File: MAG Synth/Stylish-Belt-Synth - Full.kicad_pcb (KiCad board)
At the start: 2 copper layers, 177.8 x 101.7 mm, 75 parts, among them J0 USB_B, J1 Headphone, J26 WRITE PATCH, J27 PARAM SELECT, J28 PATCH SELECT, J29 MODE, J30 STYLUS, U1 stm32f103c8t6-module-china, U2 XPT8871

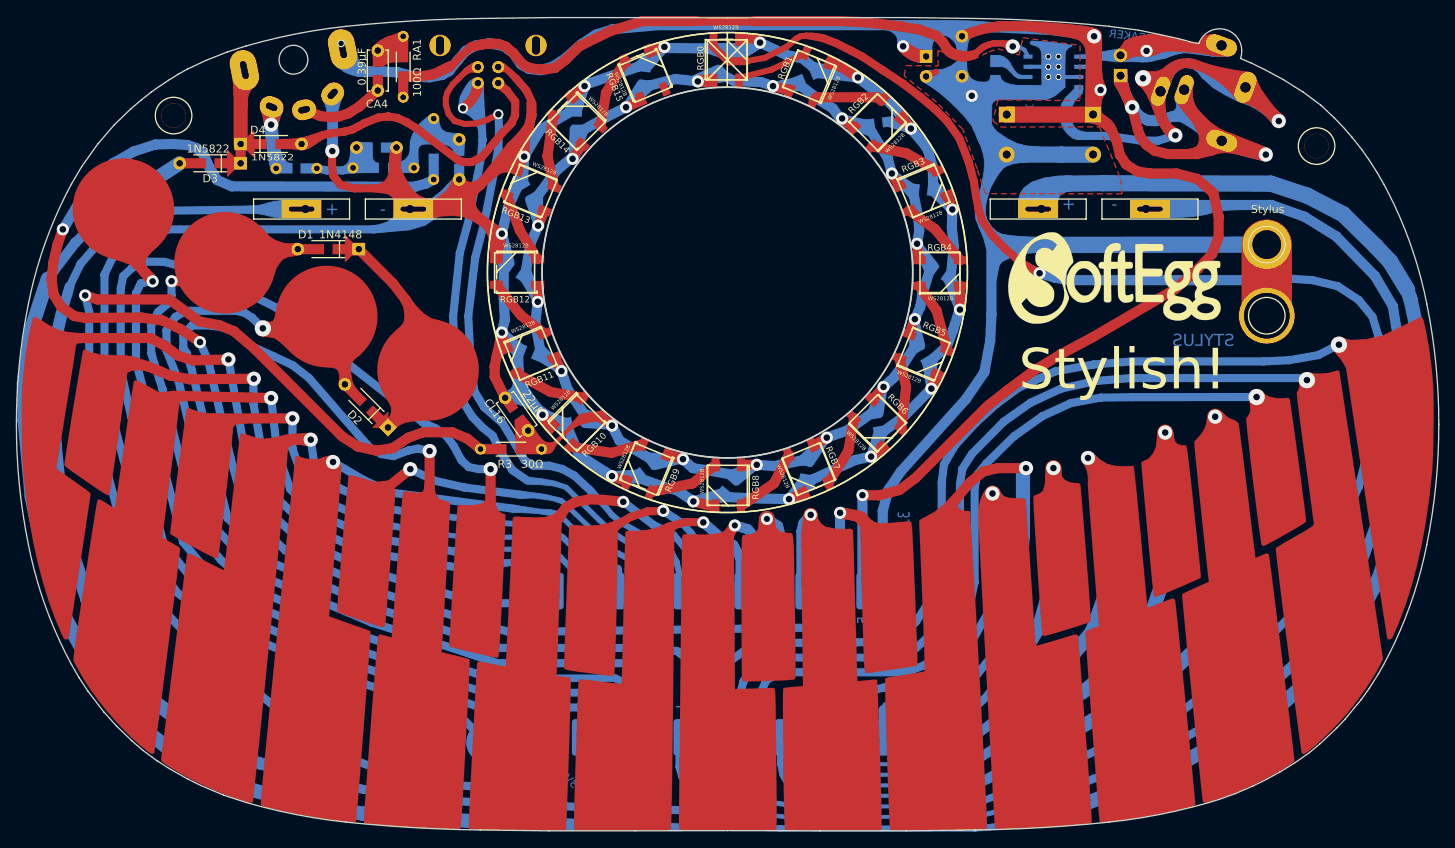
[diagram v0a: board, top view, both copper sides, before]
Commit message: Fixes for removing LED noise from the audio. Thanks Brandon for the hard work in figuring this out!
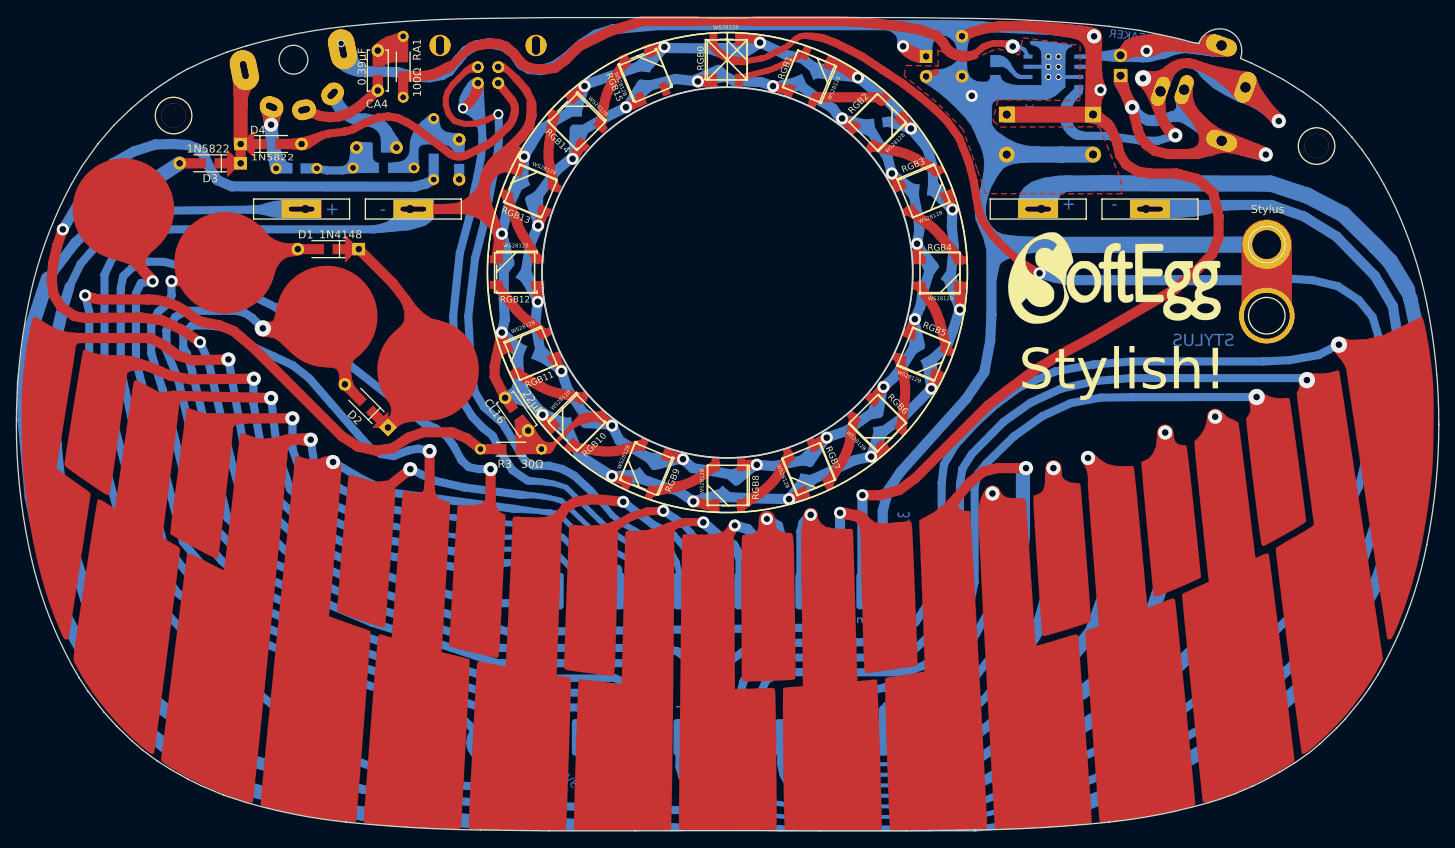
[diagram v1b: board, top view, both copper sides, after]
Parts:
- CA1: value 220μF -> 220µF
- LS1: value SPEAKER -> Speaker 4Ω 3W
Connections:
- net /DOUT renamed /WS2812B-16-LED-RING/DOUT
- BT12H1 pad 2: GND -> AGND
- BTN1 pad 1: GND -> AGND
- C1 pad 2: GND -> Net-(C1-Pad2)
- C2 pad 2: GND -> AGND
- C3 pad 2: GND -> AGND
- C4 pad 2: GND -> Net-(C4-Pad2)
- CA1 pad 2: GND -> AGND
- CA2 pad 2: GND -> AGND
- CA3 pad 2: GND -> AGND
- CL0 pad 1: /VIN -> /WS2812B-16-LED-RING/VIN
- CL0 pad 2: GND -> AGND
- CL1 pad 1: /VIN -> /WS2812B-16-LED-RING/VIN
- CL1 pad 2: GND -> AGND
- CL10 pad 1: /VIN -> /WS2812B-16-LED-RING/VIN
- CL10 pad 2: GND -> AGND
- CL11 pad 1: /VIN -> /WS2812B-16-LED-RING/VIN
- CL11 pad 2: GND -> AGND
- CL12 pad 1: /VIN -> /WS2812B-16-LED-RING/VIN
- CL12 pad 2: GND -> AGND
- CL13 pad 1: /VIN -> /WS2812B-16-LED-RING/VIN
- CL13 pad 2: GND -> AGND
- CL14 pad 1: /VIN -> /WS2812B-16-LED-RING/VIN
- CL14 pad 2: GND -> AGND
- CL15 pad 1: /VIN -> /WS2812B-16-LED-RING/VIN
- CL15 pad 2: GND -> AGND
- CL16 pad 1: /VIN -> unconnected-(CL16-Pad1)
- CL16 pad 2: GND -> AGND
- CL2 pad 1: /VIN -> /WS2812B-16-LED-RING/VIN
- CL2 pad 2: GND -> AGND
- CL3 pad 1: /VIN -> /WS2812B-16-LED-RING/VIN
- CL3 pad 2: GND -> AGND
- CL4 pad 1: /VIN -> /WS2812B-16-LED-RING/VIN
- CL4 pad 2: GND -> AGND
- CL5 pad 1: /VIN -> /WS2812B-16-LED-RING/VIN
- CL5 pad 2: GND -> AGND
- CL6 pad 1: /VIN -> /WS2812B-16-LED-RING/VIN
- CL6 pad 2: GND -> AGND
- CL7 pad 1: /VIN -> /WS2812B-16-LED-RING/VIN
- CL7 pad 2: GND -> AGND
- CL8 pad 1: /VIN -> /WS2812B-16-LED-RING/VIN
- CL8 pad 2: GND -> AGND
- CL9 pad 1: /VIN -> /WS2812B-16-LED-RING/VIN
- CL9 pad 2: GND -> AGND
- J0 pad 4: GND -> AGND
- J0 pad 5: Net-(J0-Pad5) -> unconnected-(J0-Pad5)
- J30 pad 1: GND -> AGND
- R3 pad 1: /VIN -> /WS2812B-16-LED-RING/VIN
- RGB0 pad 1: /VIN -> /WS2812B-16-LED-RING/VIN
- RGB0 pad 3: GND -> AGND
- RGB1 pad 1: /VIN -> /WS2812B-16-LED-RING/VIN
- RGB1 pad 3: GND -> AGND
- RGB10 pad 1: /VIN -> /WS2812B-16-LED-RING/VIN
- RGB10 pad 3: GND -> AGND
- RGB11 pad 1: /VIN -> /WS2812B-16-LED-RING/VIN
- RGB11 pad 3: GND -> AGND
- RGB12 pad 1: /VIN -> /WS2812B-16-LED-RING/VIN
- RGB12 pad 3: GND -> AGND
- RGB13 pad 1: /VIN -> /WS2812B-16-LED-RING/VIN
- RGB13 pad 3: GND -> AGND
- RGB14 pad 1: /VIN -> /WS2812B-16-LED-RING/VIN
- RGB14 pad 3: GND -> AGND
- RGB15 pad 1: /VIN -> /WS2812B-16-LED-RING/VIN
- RGB15 pad 3: GND -> AGND
- RGB2 pad 1: /VIN -> /WS2812B-16-LED-RING/VIN
- RGB2 pad 3: GND -> AGND
- RGB3 pad 1: /VIN -> /WS2812B-16-LED-RING/VIN
- RGB3 pad 3: GND -> AGND
- RGB4 pad 1: /VIN -> /WS2812B-16-LED-RING/VIN
- RGB4 pad 3: GND -> AGND
- RGB5 pad 1: /VIN -> /WS2812B-16-LED-RING/VIN
- RGB5 pad 3: GND -> AGND
- RGB6 pad 1: /VIN -> /WS2812B-16-LED-RING/VIN
- RGB6 pad 3: GND -> AGND
- RGB7 pad 1: /VIN -> /WS2812B-16-LED-RING/VIN
- RGB7 pad 3: GND -> AGND
- RGB8 pad 1: /VIN -> /WS2812B-16-LED-RING/VIN
- RGB8 pad 3: GND -> AGND
- RGB9 pad 1: /VIN -> /WS2812B-16-LED-RING/VIN
- RGB9 pad 3: GND -> AGND
- RV1 pad 1: GND -> Net-(C4-Pad2)
- U1 pad 19: GND -> AGND
- U1 pad 20: Net-(U1-Pad20) -> unconnected-(U1-Pad20)
- U1 pad 21: Net-(U1-Pad21) -> unconnected-(U1-Pad21)
- U1 pad 37: Net-(U1-Pad37) -> unconnected-(U1-Pad37)
- U1 pad 39: GND -> AGND
- U1 pad 40: GND -> AGND
- U2 pad 1: GND -> AGND
- U2 pad 3: GND -> AGND
- U2 pad 7: GND -> AGND
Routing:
- net GND: track 689.6 -> 0.00 mm, vias 24 -> 0
- net AGND: track 0.00 -> 642.0 mm, vias 0 -> 23
- net /WS2812B-16-LED-RING/VIN: track 0.00 -> 262.7 mm, vias 0 -> 16
- net /VIN: track 262.7 -> 0.00 mm, vias 16 -> 0
- net Net-(C4-Pad2): track 0.00 -> 11.0 mm
- net Net-(D4-Pad2): track 36.7 -> 35.5 mm
- added copper zone on F.Cu, net AGND
- removed copper zone on F.Cu, net GND
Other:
- net class Default removed
- board text added: "Connect"

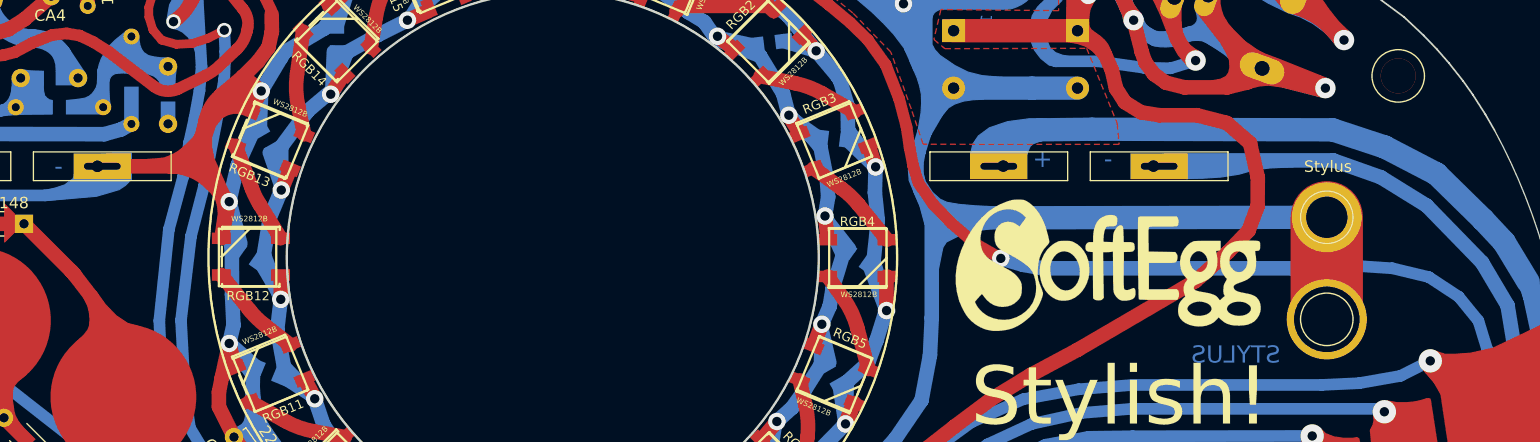
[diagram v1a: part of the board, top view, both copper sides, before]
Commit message: Updated fix for audio problems, adds AGND to C4 too. 3d models for parts extracted from old PCB model - only partly complete
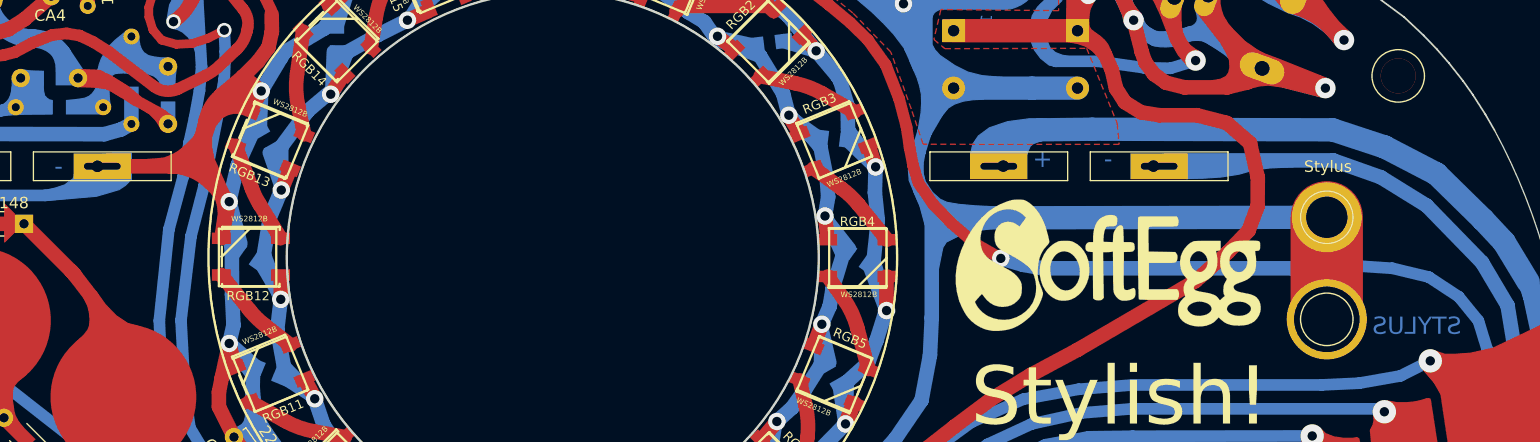
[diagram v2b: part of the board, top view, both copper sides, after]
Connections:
- C1 pad 2: Net-(C1-Pad2) -> Net-(C4-Pad2)
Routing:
- net Net-(C4-Pad2): track 11.0 -> 20.2 mm

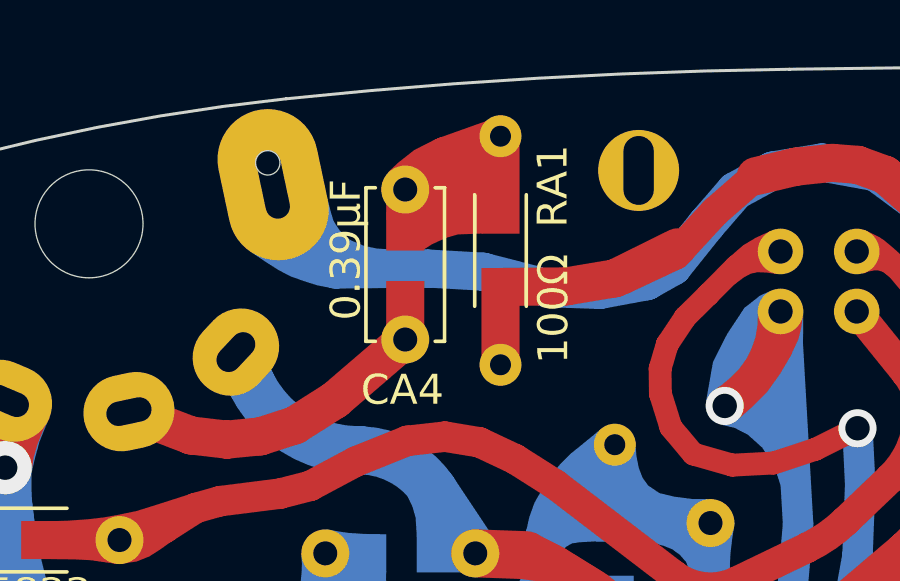
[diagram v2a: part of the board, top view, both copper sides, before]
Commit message: PCB now probably matches schematic. 3d parts now mostly centered 3d parts all updated and should appear properly if not, make sure to adjust the directories for your system, because I don't know how to redirect them better
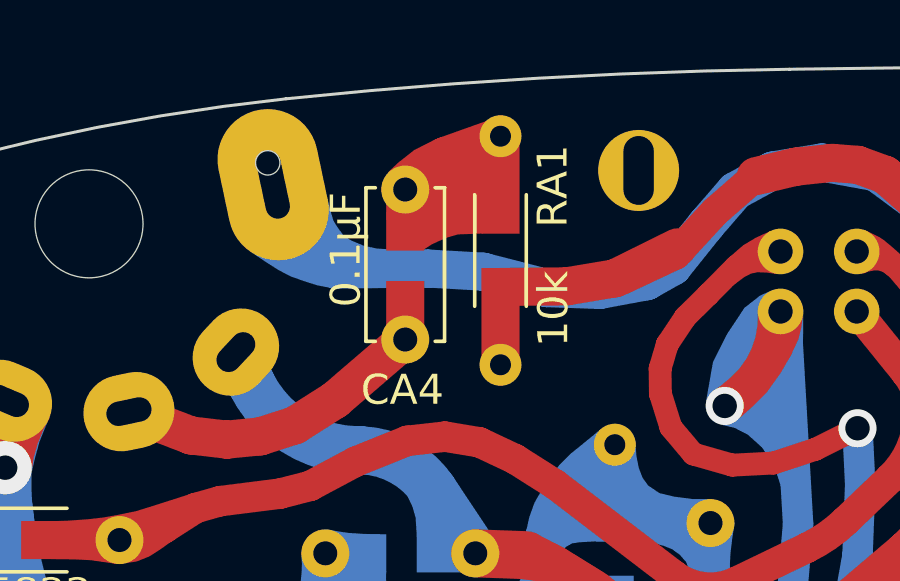
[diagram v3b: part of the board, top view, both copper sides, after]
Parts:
- CA4: value 0.39μF -> 0.1μF
- RA1: value 100Ω -> 10k
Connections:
- net /+3.3V renamed +3.3V
- net /+5V renamed +5V
- net Net-(C4-Pad2) renamed GNDA
- net Net-(J1-Pad3) renamed /LS-
- net Net-(J1-Pad4) renamed /LS+
- BT12H1 pad 2: AGND -> GND
- BTN1 pad 1: AGND -> GND
- C2 pad 2: AGND -> GND
- C3 pad 2: AGND -> GND
- CA1 pad 2: AGND -> GND
- CA2 pad 2: AGND -> GND
- CA3 pad 2: AGND -> GND
- CL0 pad 2: AGND -> GND
- CL1 pad 2: AGND -> GND
- CL10 pad 2: AGND -> GND
- CL11 pad 2: AGND -> GND
- CL12 pad 2: AGND -> GND
- CL13 pad 2: AGND -> GND
- CL14 pad 2: AGND -> GND
- CL15 pad 2: AGND -> GND
- CL16 pad 1: unconnected-(CL16-Pad1) -> /WS2812B-16-LED-RING/VIN
- CL16 pad 2: AGND -> GND
- CL2 pad 2: AGND -> GND
- CL3 pad 2: AGND -> GND
- CL4 pad 2: AGND -> GND
- CL5 pad 2: AGND -> GND
- CL6 pad 2: AGND -> GND
- CL7 pad 2: AGND -> GND
- CL8 pad 2: AGND -> GND
- CL9 pad 2: AGND -> GND
- D3 pad 1: /VUSB -> Net-(D3-K)
- D4 pad 1: /VUSB -> Net-(D3-K)
- D4 pad 2: Net-(D4-Pad2) -> /VUSB
- J0 pad 1: Net-(D4-Pad2) -> /VUSB
- J0 pad 4: AGND -> GND
- J30 pad 1: AGND -> GND
- RGB0 pad 3: AGND -> GND
- RGB1 pad 3: AGND -> GND
- RGB10 pad 3: AGND -> GND
- RGB11 pad 3: AGND -> GND
- RGB12 pad 3: AGND -> GND
- RGB13 pad 3: AGND -> GND
- RGB14 pad 3: AGND -> GND
- RGB15 pad 3: AGND -> GND
- RGB2 pad 3: AGND -> GND
- RGB3 pad 3: AGND -> GND
- RGB4 pad 3: AGND -> GND
- RGB5 pad 3: AGND -> GND
- RGB6 pad 3: AGND -> GND
- RGB7 pad 3: AGND -> GND
- RGB8 pad 3: AGND -> GND
- RGB9 pad 3: AGND -> GND
- RV1 pad 5: /VUSB -> Net-(D3-K)
- U1 pad 19: AGND -> GND
- U1 pad 39: AGND -> GND
- U1 pad 40: AGND -> GND
- U2 pad 1: AGND -> GND
- U2 pad 3: AGND -> GND
- U2 pad 7: AGND -> GND
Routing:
- net GND: track 0.00 -> 642.0 mm, vias 0 -> 23
- net AGND: track 642.0 -> 0.00 mm, vias 23 -> 0
- net Net-(D4-Pad2): track 35.5 -> 0.00 mm
- net /VUSB: track 15.5 -> 35.5 mm
- net Net-(D3-K): track 0.00 -> 15.5 mm
- added copper zone on F.Cu, net +5V
- removed copper zone on F.Cu, net AGND
